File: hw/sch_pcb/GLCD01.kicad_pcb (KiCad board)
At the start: 2 copper layers, 40.1 x 40.1 mm, 15 parts, among them J1 JUMP_7X2, J2 046824610000846+, M1 HOLE M3, M2 HOLE M3, M3 HOLE, M4 HOLE, Q1 BSS138, U1 MIC1557YM5-TR

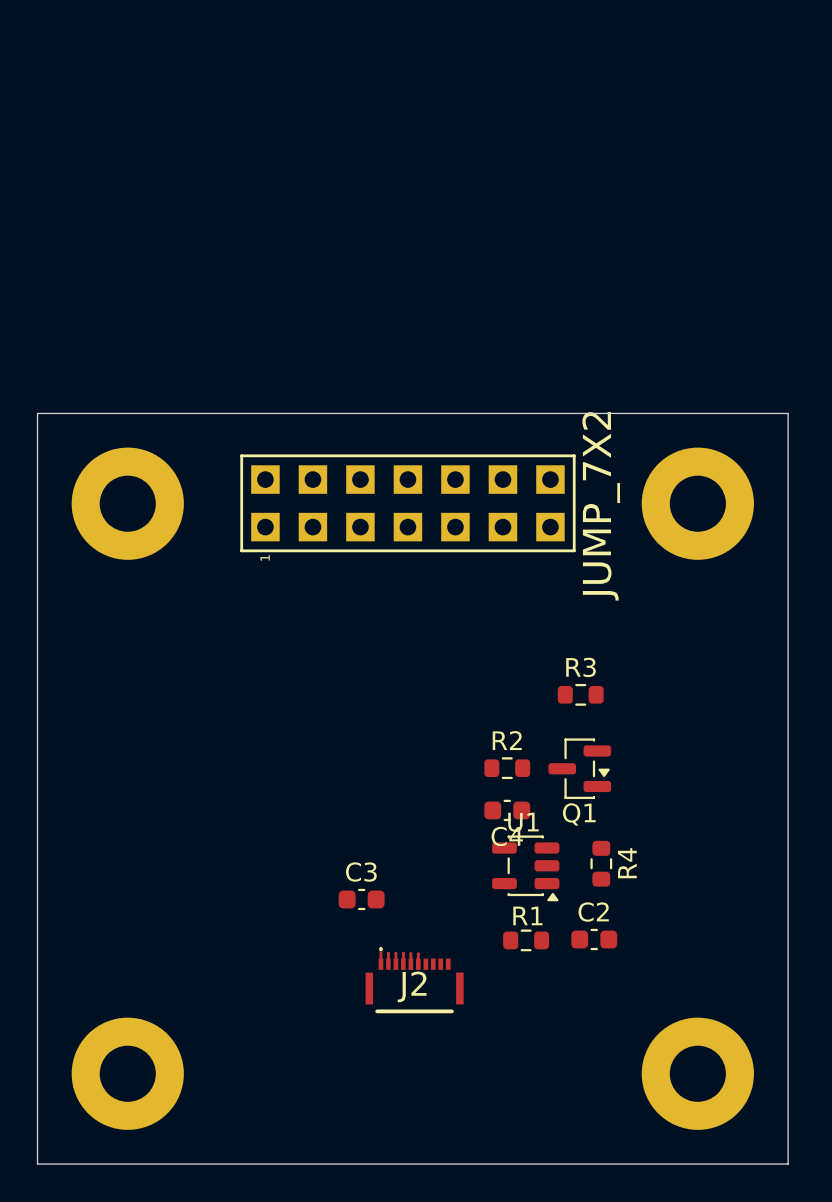
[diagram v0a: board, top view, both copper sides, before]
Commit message: Add MIC1557 circuit to schematic and update PCB layout
- Added R5 (0R, DNP) resistor to schematic
- Rearranged component placement on PCB
- Updated project file to newer KiCAD format
- Fixed author email in schematic title block
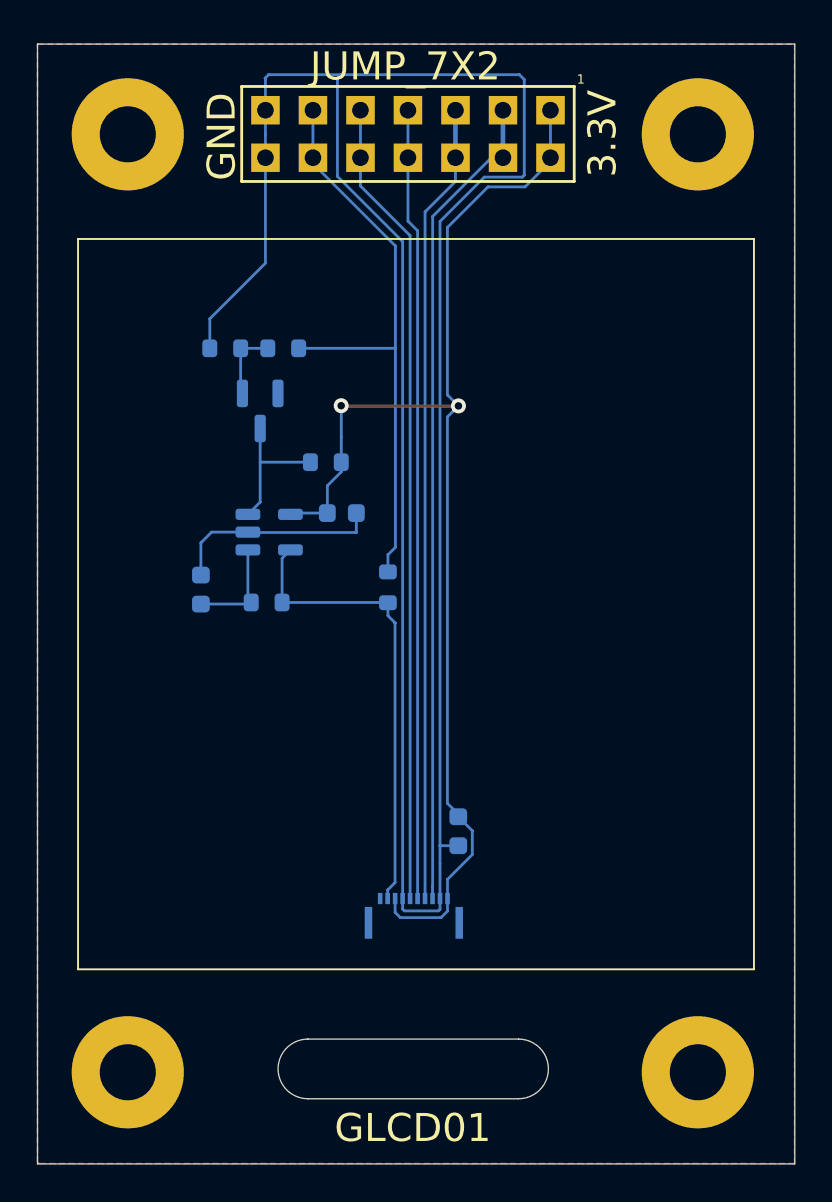
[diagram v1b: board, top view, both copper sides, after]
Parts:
- added R5: 0R, Resistor_SMD:R_0603_1608Metric, B.Cu at (125.7, 85.8)
- C2, C3, C4, J2, Q1, R1, R2, R3, R4, U1: moved to B.Cu
- moved R4 34.1 mm to (117.0, 73.0), turned to 180 degrees
- moved C2 28.1 mm to (115.7, 85.9), turned to 90 degrees
- moved Q1 25.7 mm to (118.8, 76.3), turned to -90 degrees
- moved R3 24.4 mm to (120.1, 73.0), turned to 180 degrees
- moved R1 22.8 mm to (119.2, 86.6), turned to 180 degrees
- moved U1 22.5 mm to (119.3, 82.8), turned to 0 degrees
- moved C3 20.7 mm to (123.2, 81.8)
- moved J1 19.8 mm to (126.7, 61.5), turned to -90 degrees
- moved M1 19.8 mm to (142.2, 61.5)
- moved M2 19.8 mm to (111.8, 61.5)
- moved R2 19.0 mm to (122.3, 79.1), turned to 180 degrees
- moved J2 3.51 mm to (127.1, 103.7), turned to 180 degrees
- moved C4 2.85 mm to (129.4, 98.8), turned to -90 degrees
- moved M3 0.08 mm to (111.8, 111.7)
- moved M4 0.08 mm to (142.2, 111.7)
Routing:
- net GND: track 0.59 -> 137.7 mm
- net +3.3V: track 0.87 -> 65.9 mm, vias 0 -> 2
- net Net-(J1-4-Pad3): track 0.57 -> 44.1 mm
- net Net-(J1-10-Pad9): track 0.55 -> 43.2 mm
- net Net-(J1-6-Pad5): track 0.59 -> 42.8 mm
- net Net-(J1-8-Pad7): track 0.56 -> 42.4 mm
- net Net-(J1-12-Pad11): track 0.00 -> 31.9 mm
- net Net-(U1-OUT): track 0.00 -> 24.8 mm
- net Net-(Q1-D): track 0.00 -> 7.56 mm
- net Net-(U1-T/T): track 0.00 -> 5.61 mm
- net Net-(Q1-G): track 0.00 -> 3.90 mm
- added copper zone on B.Cu, net GND
- added copper zone on F.Cu, net GND
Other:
- board size 40.1 x 40.1 mm -> 40.5 x 59.9 mm
- board text added: "3.3V"
- board text added: "GLCD01"
- board text added: "GND"

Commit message: Update PCB layout and tighten DRC rules
Reduced clearance and hole constraints for denser routing.
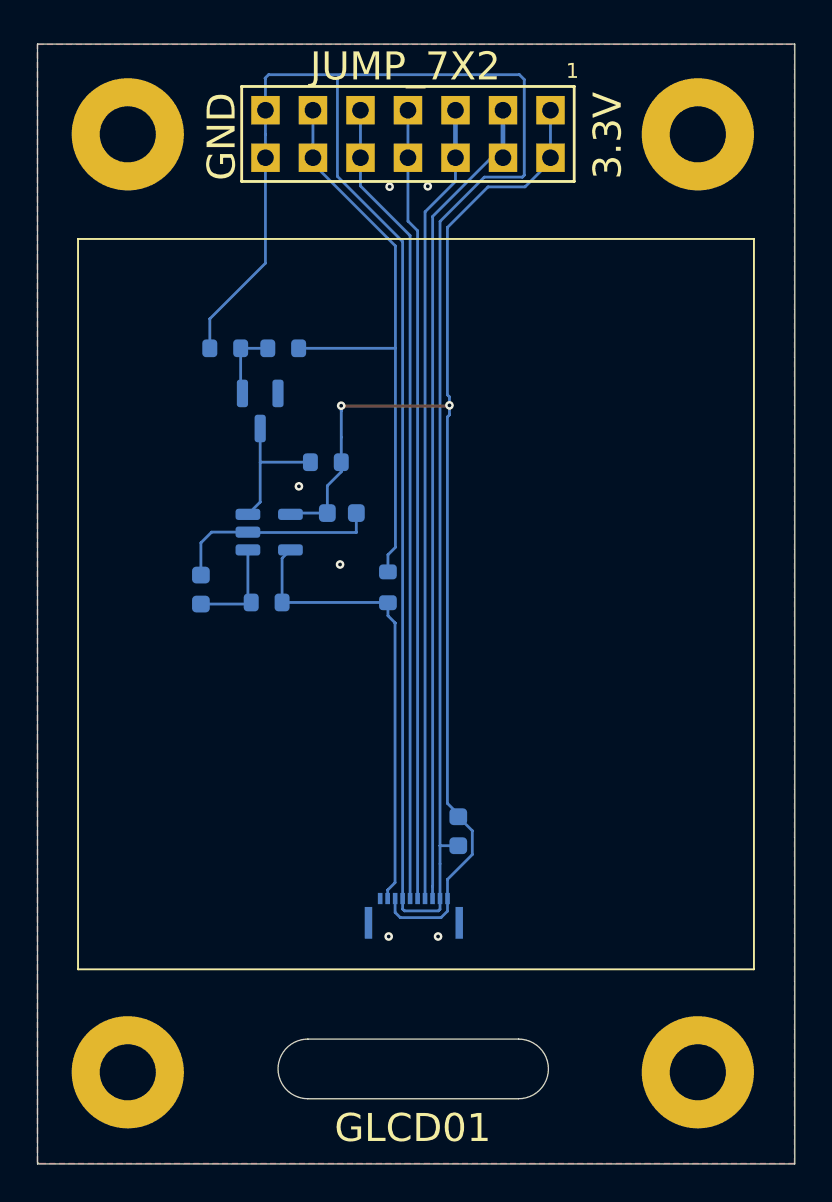
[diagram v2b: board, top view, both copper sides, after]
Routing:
- net +3.3V: track 65.9 -> 65.0 mm
- net GND: vias 0 -> 6
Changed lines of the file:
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@@
 		)
 		(fp_text user "1"
-			(at -2.921 -9.24 180)
+			(at -3.37 -8.79 180)
 			(layer "F.SilkS")
 			(effects
 				(font
-					(size 0.5 0.5)
-					(thickness 0.05)
+					(size 0.8 0.8)
+					(thickness 0.08)
 				)
 			)
@@
 	)
 	(gr_text "3.3V"
-		(at 137.14 63.83 90)
+		(at 137.42 63.94 90)
 		(layer "F.SilkS")
 		(effects
@@
 		(net 1)
 	)
+	(via
+		(at 127.8 64.31)
+		(size 0.46)
+		(drill 0.2)
+		(layers "F.Cu" "B.Cu")
+		(free yes)
+		(net 2)
+	)
+	(via
+		(at 125.76 64.33)
+		(size 0.46)
+		(drill 0.2)
+		(layers "F.Cu" "B.Cu")
+		(free yes)
+		(net 2)
+	)
+	(via
+		(at 120.91 80.35)
+		(size 0.46)
+		(drill 0.2)
+		(layers "F.Cu" "B.Cu")
+		(free yes)
+		(net 2)
+	)
+	(via
+		(at 125.71 104.42)
+		(size 0.46)
+		(drill 0.2)
+		(layers "F.Cu" "B.Cu")
+		(free yes)
+		(net 2)
+	)
+	(via
+		(at 123.11 84.53)
+		(size 0.46)
+		(drill 0.2)
+		(layers "F.Cu" "B.Cu")
+		(free yes)
+		(net 2)
+	)
+	(via
+		(at 128.35 104.42)
+		(size 0.46)
+		(drill 0.2)
+		(layers "F.Cu" "B.Cu")
+		(free yes)
+		(net 2)
+	)
 	(segment
 		(start 123.16 58.34)
@@
 	(segment
 		(start 123.19 76.06)
-		(end 129.43 76.06)
+		(end 123.17 76.04)
 		(width 0.15)
 		(layer "F.Cu")
@@
 	)
 	(segment
-		(start 123.17 76.04)
+		(start 128.92 76.06)
 		(end 123.19 76.06)
 		(width 0.15)
@@
 	)
 	(segment
-		(start 129.43 76.06)
-		(end 129.44 76.05)
+		(start 128.96 76.02)
+		(end 128.92 76.06)
 		(width 0.15)
 		(layer "F.Cu")
@@
 	(via
 		(at 123.17 76.04)
-		(size 0.8)
-		(drill 0.4)
+		(size 0.46)
+		(drill 0.2)
 		(layers "F.Cu" "B.Cu")
 		(net 3)
 	)
 	(via
-		(at 129.44 76.05)
-		(size 0.8)
-		(drill 0.4)
+		(at 128.96 76.02)
+		(size 0.46)
+		(drill 0.2)
 		(layers "F.Cu" "B.Cu")
 		(net 3)
@@
 	)
 	(segment
-		(start 130.181 98.766)
-		(end 129.43 98.015)
-		(width 0.15)
-		(layer "B.Cu")
-		(net 3)
-	)
-	(segment
-		(start 126.055 103.135)
-		(end 126.33 103.41)
+		(start 128.96 76.02)
+		(end 128.96 75.57)
 		(width 0.15)
 		(layer "B.Cu")
@@
 	)
 	(segment
-		(start 128.855 102.39)
-		(end 128.855 101.365)
+		(start 128.85 97.3)
+		(end 129.43 97.88)
 		(width 0.15)
 		(layer "B.Cu")
@@
 	)
 	(segment
-		(start 120.5275 81.78)
-		(end 120.4575 81.85)
+		(start 130.181 98.766)
+		(end 129.43 98.015)
 		(width 0.15)
 		(layer "B.Cu")
@@
 	)
 	(segment
-		(start 128.85 76.64)
-		(end 129.44 76.05)
+		(start 128.96 75.57)
+		(end 128.85 75.46)
 		(width 0.15)
 		(layer "B.Cu")
@@
 	)
 	(segment
-		(start 131.02 64.34)
-		(end 133 64.34)
+		(start 126.055 103.135)
+		(end 126.33 103.41)
 		(width 0.15)
 		(layer "B.Cu")
@@
 	)
 	(segment
-		(start 128.855 103.063388)
-		(end 128.855 102.39)
+		(start 128.855 102.39)
+		(end 128.855 101.365)
 		(width 0.15)
 		(layer "B.Cu")
@@
 	)
 	(segment
-		(start 123.175 76.315)
-		(end 123.175 77.73)
+		(start 120.5275 81.78)
+		(end 120.4575 81.85)
 		(width 0.15)
 		(layer "B.Cu")
@@
 	)
 	(segment
-		(start 128.85 97.3)
-		(end 128.85 76.64)
+		(start 128.855 103.063388)
+		(end 128.855 102.39)
 		(width 0.15)
 		(layer "B.Cu")
@@
 	)
 	(segment
-		(start 133 64.34)
-		(end 134.36 62.98)
+		(start 123.175 76.315)
+		(end 123.175 77.73)
 		(width 0.15)
 		(layer "B.Cu")
@@
 	)
 	(segment
-		(start 129.44 76.05)
-		(end 128.85 75.46)
+		(start 128.85 76.64)
+		(end 128.85 97.3)
+		(width 0.15)
+		(layer "B.Cu")
+		(net 3)
+	)
+	(segment
+		(start 131.02 64.34)
+		(end 133 64.34)
 		(width 0.15)
 		(layer "B.Cu")
@@
 	)
 	(segment
-		(start 123.175 77.73)
-		(end 123.175 79.575)
+		(start 128.85 66.51)
+		(end 131.02 64.34)
 		(width 0.15)
 		(layer "B.Cu")
@@
 	)
 	(segment
-		(start 128.85 75.46)
-		(end 128.85 66.51)
+		(start 123.175 77.73)
+		(end 123.175 79.575)
 		(width 0.15)
 		(layer "B.Cu")
@@
 	)
 	(segment
-		(start 129.43 97.88)
-		(end 128.85 97.3)
+		(start 134.36 62.98)
+		(end 134.36 62.78)
 		(width 0.15)
 		(layer "B.Cu")
@@
 	)
 	(segment
-		(start 128.85 66.51)
-		(end 131.02 64.34)
+		(start 128.85 75.46)
+		(end 128.85 66.51)
 		(width 0.15)
 		(layer "B.Cu")
@@
 	)
 	(segment
-		(start 134.36 62.98)
-		(end 134.36 62.78)
+		(start 128.96 76.53)
+		(end 128.85 76.64)
 		(width 0.15)
 		(layer "B.Cu")
@@
 	)
 	(segment
+		(start 128.96 76.02)
+		(end 128.96 76.53)
+		(width 0.15)
+		(layer "B.Cu")
+		(net 3)
+	)
+	(segment
+		(start 133 64.34)
+		(end 134.36 62.98)
+		(width 0.15)
+		(layer "B.Cu")
+		(net 3)
+	)
+	(segment
 		(start 120.895 72.97)
 		(end 126.06 72.97)
@@
 		(width 0.15)
 		(layer "B.Cu")
-		(net 4)
-	)
-	(segment
-		(start 126.06 72.97)
-		(end 126.07 72.98)
-		(width 0.15)
-		(layer "B.Cu")

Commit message: fix schematics, improve layout, thicker traces, update layout, add polarity protection, ...
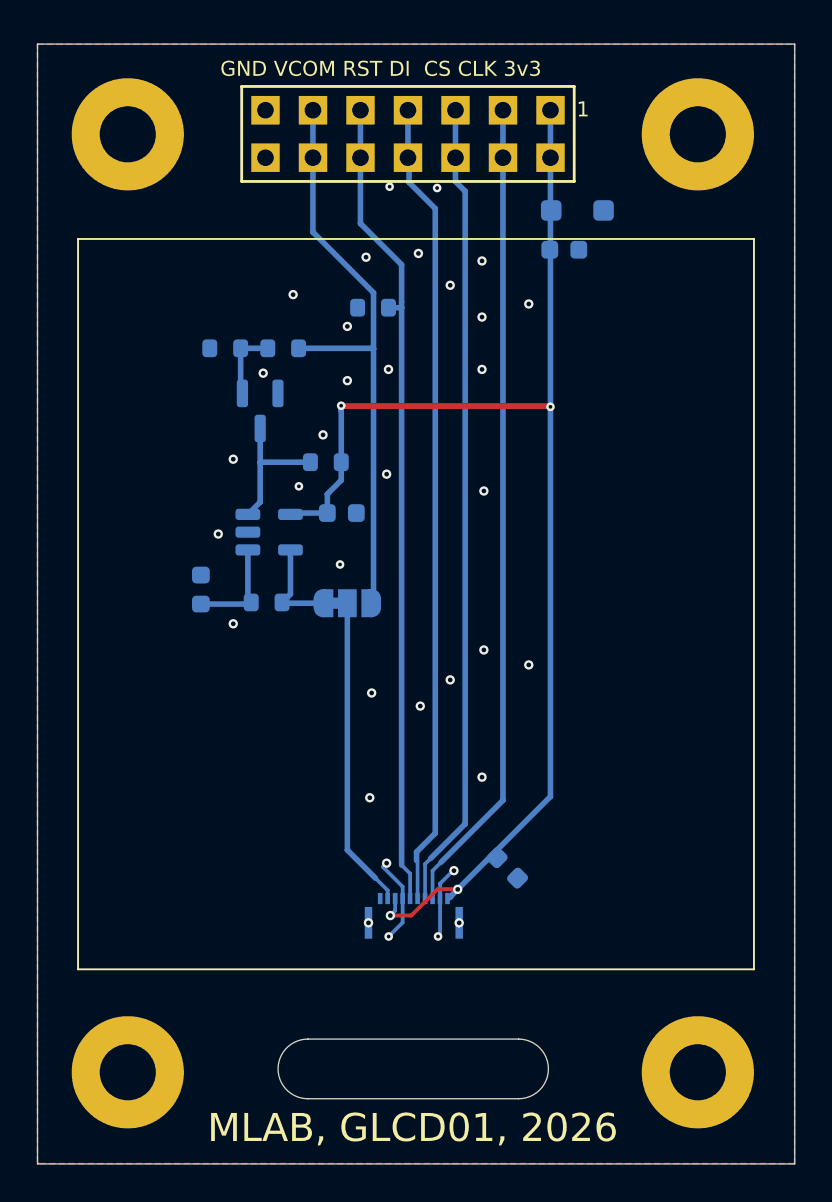
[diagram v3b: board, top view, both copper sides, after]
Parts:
- added C1: 10u, Capacitor_SMD:C_0603_1608Metric, B.Cu at (135.1, 67.7)
- added D2: BZT52H-C3V6,115, Diode_SMD:D_SOD-123F, B.Cu at (135.8, 65.6)
- added JP1: SolderJumper_3_Bridged12, Jumper:SolderJumper-3_P1.3mm_Bridged12_RoundedPad1.0x1.5mm, B.Cu at (123.5, 86.6)
- C3, C4: value 100nF/63V -> 100n
- R5: value 0R -> 10k
- moved R5 15.0 mm to (124.9, 70.8), turned to 0 degrees
- moved C4 3.27 mm to (132.1, 100.8), turned to -45 degrees
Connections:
- net Net-(J1-4-Pad3) renamed /SCLK
- net Net-(J1-6-Pad5) renamed /SCS
- net Net-(J1-8-Pad7) renamed /SI
- J1 pad 10: Net-(J1-10-Pad9) -> /RST
- J1 pad 11: Net-(J1-12-Pad11) -> /VCOM_CTRL
- J1 pad 12: Net-(J1-12-Pad11) -> /VCOM_CTRL
- J1 pad 9: Net-(J1-10-Pad9) -> /RST
- J2 pad 6: Net-(J1-10-Pad9) -> /RST
- J2 pad 9: Net-(U1-OUT) -> /VCOM
- J2 pad MP1: unconnected-(J2-PadMP1) -> GND
- J2 pad MP2: unconnected-(J2-PadMP2) -> GND
- R1 pad 1: Net-(U1-OUT) -> /1hz
- R3 pad 1: Net-(J1-12-Pad11) -> /VCOM_CTRL
- R5 pad 1: Net-(J1-12-Pad11) -> GND
- R5 pad 2: Net-(U1-OUT) -> /RST
- U1 pad 5: Net-(U1-OUT) -> /1hz
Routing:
- net GND: track 137.7 -> 8.68 mm, vias 6 -> 35
- net /RST: track 0.00 -> 43.9 mm
- net Net-(J1-10-Pad9): track 43.2 -> 0.00 mm
- net Net-(J1-12-Pad11): track 31.8 -> 0.00 mm
- net /VCOM_CTRL: track 0.00 -> 31.8 mm
- net Net-(U1-OUT): track 24.8 -> 0.00 mm
- net /VCOM: track 0.00 -> 16.7 mm
- net /1hz: track 0.00 -> 5.20 mm
- net +3.3V: track 65.0 -> 68.7 mm, vias 2 -> 4
- net /SI: track 42.4 -> 43.1 mm
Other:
- board text added: "3v3 CLK CS DI RST VCOM GND"
- board text added: "GND VCOM RST DI CS CLK 3v3"
- board text added: "MLAB, GLCD01, 2026"
- board text removed: "3.3V"
- board text removed: "GLCD01"
- board text removed: "GND"
